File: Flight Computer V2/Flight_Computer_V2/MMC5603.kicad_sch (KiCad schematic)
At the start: 8 parts, among them IC6 MMC5603NJ

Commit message: finalized schematic, added datasheets, and pdf of schematic
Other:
- company: (none) -> By: Dylan Haussecker
- title: (none) -> Avionics Flight Computer
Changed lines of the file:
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@@
 (kicad_sch (version 20230121) (generator eeschema)
   (paper "A4")
+  (title_block
+    (title "Avionics Flight Computer")
+    (date "2023-09-04")
+    (rev "1.0")
+    (company "By: Dylan Haussecker")
+  )
   (junction (at 173.99 90.17) (diameter 0) (color 0 0 0 0)
   )

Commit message: updated pcb
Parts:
- C20: footprint (none) -> Capacitor_SMD:C_0603_1608Metric
- IC6: footprint MMC5603NJ -> LibraryLoader:MMC5603NJ
- JP3: footprint (none) -> Jumper:SolderJumper-2_P1.3mm_Open_Pad1.0x1.5mm
- R22: footprint (none) -> Resistor_SMD:R_0402_1005Metric
- R23: footprint (none) -> Resistor_SMD:R_01005_0402Metric
- TP3: footprint (none) -> TestPoint:TestPoint_Pad_D1.0mm
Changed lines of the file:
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@@
       (effects (font (size 1.27 1.27)))
     )
-    (property "Footprint" "MMC5603NJ" (at 149.86 87.63 0)
+    (property "Footprint" "LibraryLoader:MMC5603NJ" (at 149.86 87.63 0)
       (effects (font (size 1.27 1.27)) (justify left) hide)
     )
@@
       (effects (font (size 1.27 1.27)) (justify left))
     )
-    (property "Footprint" "" (at 190.5 83.82 0)
+    (property "Footprint" "Resistor_SMD:R_01005_0402Metric" (at 190.5 83.82 0)
       (effects (font (size 1.27 1.27)) hide)
     )
@@
       (effects (font (size 1.27 1.27)))
     )
-    (property "Footprint" "" (at 180.34 90.17 0)
+    (property "Footprint" "Jumper:SolderJumper-2_P1.3mm_Open_Pad1.0x1.5mm" (at 180.34 90.17 0)
       (effects (font (size 1.27 1.27)) hide)
     )
@@
       (effects (font (size 1.27 1.27)) (justify left) hide)
     )
-    (property "Footprint" "" (at 179.07 88.9 0)
+    (property "Footprint" "TestPoint:TestPoint_Pad_D1.0mm" (at 179.07 88.9 0)
       (effects (font (size 1.27 1.27)) hide)
     )
@@
       (effects (font (size 1.27 1.27)) (justify left))
     )
-    (property "Footprint" "" (at 158.75 83.82 0)
+    (property "Footprint" "Resistor_SMD:R_0402_1005Metric" (at 158.75 83.82 0)
       (effects (font (size 1.27 1.27)) hide)
     )
@@
       (effects (font (size 1.27 1.27)) (justify left) hide)
     )
-    (property "Footprint" "" (at 200.66 91.44 0)
+    (property "Footprint" "TestPoint:TestPoint_Pad_D1.0mm" (at 200.66 91.44 0)
       (effects (font (size 1.27 1.27)) hide)
     )
@@
       (effects (font (size 1.27 1.27)) (justify left))
     )
-    (property "Footprint" "" (at 128.27 102.87 0)
+    (property "Footprint" "Capacitor_SMD:C_0603_1608Metric" (at 128.27 102.87 0)
       (effects (font (size 1.27 1.27)) hide)
     )
@@
       (effects (font (size 1.27 1.27)))
     )
-    (property "Footprint" "" (at 201.93 92.71 0)
-      (effects (font (size 1.27 1.27)) hide)
-    )
+    (property "Footprint" "Jumper:SolderJumper-2_P1.3mm_Open_Pad1.0x1.5mm" (at 201.93 92.71 0)
+      (effects (font (size 1.27 1.27)) hide)
+    )

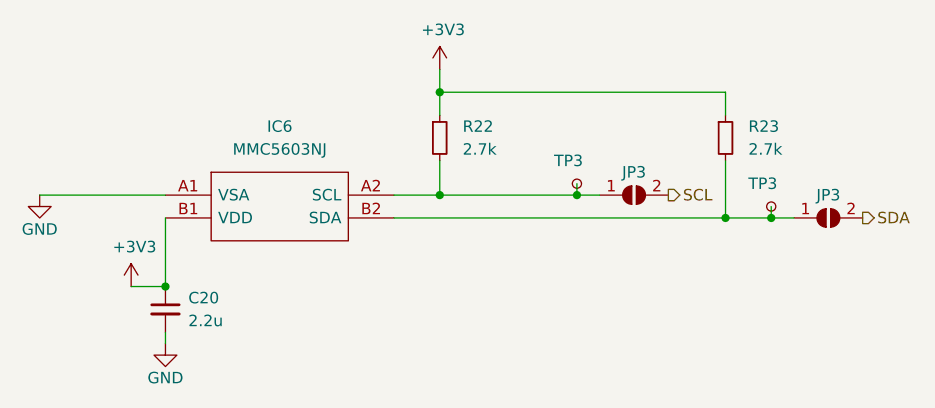
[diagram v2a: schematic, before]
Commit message: changed new flight computer scl resistors
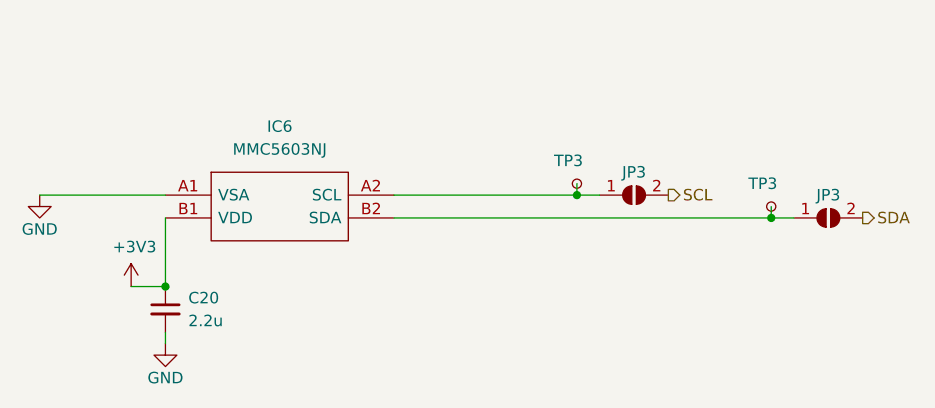
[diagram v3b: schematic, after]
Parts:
- removed R22: 2.7k, Resistor_SMD:R_0402_1005Metric, symbol Device:R_Small
- removed R23: 2.7k, Resistor_SMD:R_01005_0402Metric, symbol Device:R_Small
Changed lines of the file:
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@@
   (junction (at 173.99 90.17) (diameter 0) (color 0 0 0 0)
   )
-  (junction (at 190.5 92.71) (diameter 0) (color 0 0 0 0)
-  )
-  (junction (at 158.75 78.74) (diameter 0) (color 0 0 0 0)
-  )
   (junction (at 128.27 100.33) (diameter 0) (color 0 0 0 0)
   )
-  (junction (at 158.75 90.17) (diameter 0) (color 0 0 0 0)
-  )
   (junction (at 195.58 92.71) (diameter 0) (color 0 0 0 0)
   )
@@
     (stroke (width 0) (type default))
   )
-  (wire (pts (xy 190.5 81.28) (xy 190.5 78.74))
-    (stroke (width 0) (type default))
-  )
-  (wire (pts (xy 158.75 86.36) (xy 158.75 90.17))
-    (stroke (width 0) (type default))
-  )
   (wire (pts (xy 124.46 100.33) (xy 128.27 100.33))
     (stroke (width 0) (type default))
   )
-  (wire (pts (xy 158.75 76.2) (xy 158.75 78.74))
-    (stroke (width 0) (type default))
-  )
   (wire (pts (xy 128.27 105.41) (xy 128.27 106.68))
     (stroke (width 0) (type default))
   )
-  (wire (pts (xy 190.5 78.74) (xy 158.75 78.74))
-    (stroke (width 0) (type default))
-  )
   (wire (pts (xy 173.99 88.9) (xy 173.99 90.17))
     (stroke (width 0) (type default))
@@
     (stroke (width 0) (type default))
   )
-  (wire (pts (xy 158.75 90.17) (xy 173.99 90.17))
-    (stroke (width 0) (type default))
-  )
-  (wire (pts (xy 190.5 92.71) (xy 190.5 86.36))
+  (wire (pts (xy 153.67 90.17) (xy 173.99 90.17))
     (stroke (width 0) (type default))
   )
@@
     (stroke (width 0) (type default))
   )
-  (wire (pts (xy 190.5 92.71) (xy 195.58 92.71))
-    (stroke (width 0) (type default))
-  )
-  (wire (pts (xy 158.75 78.74) (xy 158.75 81.28))
-    (stroke (width 0) (type default))
-  )
-  (wire (pts (xy 153.67 92.71) (xy 190.5 92.71))
-    (stroke (width 0) (type default))
-  )
-  (wire (pts (xy 153.67 90.17) (xy 158.75 90.17))
+  (wire (pts (xy 153.67 92.71) (xy 195.58 92.71))
     (stroke (width 0) (type default))
   )
@@
     )
   )
-  (symbol (lib_id "Device:R_Small") (at 190.5 83.82 0) (unit 1)
-    (in_bom yes) (on_board yes) (dnp no) (fields_autoplaced)
-    (property "Reference" "R23" (at 193.04 82.55 0)
-      (effects (font (size 1.27 1.27)) (justify left))
-    )
-    (property "Value" "2.7k" (at 193.04 85.09 0)
-      (effects (font (size 1.27 1.27)) (justify left))
-    )
-    (property "Footprint" "Resistor_SMD:R_01005_0402Metric" (at 190.5 83.82 0)
-      (effects (font (size 1.27 1.27)) hide)
-    )
-    (property "Datasheet" "~" (at 190.5 83.82 0)
-      (effects (font (size 1.27 1.27)) hide)
-    )
-    (pin "1")
-    (pin "2")
-    (instances
-      (project "Flight_Computer_V2"
-        (path "/39d7ebb3-b69d-4ae9-8f55-c9acfe77d345/82e19a29-2001-4834-a54c-a35440bfa66f"
-          (reference "R23") (unit 1)
-        )
-      )
-    )
-  )
   (symbol (lib_id "Jumper:SolderJumper_2_Open") (at 180.34 90.17 0) (unit 1)
     (in_bom yes) (on_board yes) (dnp no)
@@
         (path "/b1d299c5-d712-4abd-abfc-85bf9dc0241e/b49ccfa2-a443-40e6-a4d4-e4cbe0c6bead"
           (reference "#PWR020") (unit 1)
-        )
-      )
-    )
-  )
-  (symbol (lib_id "Device:R_Small") (at 158.75 83.82 0) (unit 1)
-    (in_bom yes) (on_board yes) (dnp no) (fields_autoplaced)
-    (property "Reference" "R22" (at 161.29 82.55 0)
-      (effects (font (size 1.27 1.27)) (justify left))
-    )
-    (property "Value" "2.7k" (at 161.29 85.09 0)
-      (effects (font (size 1.27 1.27)) (justify left))
-    )
-    (property "Footprint" "Resistor_SMD:R_0402_1005Metric" (at 158.75 83.82 0)
-      (effects (font (size 1.27 1.27)) hide)
-    )
-    (property "Datasheet" "~" (at 158.75 83.82 0)
-      (effects (font (size 1.27 1.27)) hide)
-    )
-    (pin "1")
-    (pin "2")
-    (instances
-      (project "Flight_Computer_V2"
-        (path "/39d7ebb3-b69d-4ae9-8f55-c9acfe77d345/82e19a29-2001-4834-a54c-a35440bfa66f"
-          (reference "R22") (unit 1)
         )
       )
@@
         )
       )
-    )
-  )
-  (symbol (lib_id "power:+3V3") (at 158.75 76.2 0) (unit 1)
-    (in_bom yes) (on_board yes) (dnp no)
-    (property "Reference" "#PWR09" (at 158.75 80.01 0)
-      (effects (font (size 1.27 1.27)) hide)
-    )
-    (property "Value" "+3V3" (at 159.131 71.8058 0)
-      (effects (font (size 1.27 1.27)))
-    )
-    (property "Footprint" "" (at 158.75 76.2 0)
-      (effects (font (size 1.27 1.27)) hide)
-    )
-    (property "Datasheet" "" (at 158.75 76.2 0)
-      (effects (font (size 1.27 1.27)) hide)
-    )
-    (pin "1")
-    (instances
-      (project "STM32F405RGT6-Breakout"
-        (path "/0540e924-c3ed-4064-b360-826f481ae85c"
-          (reference "#PWR09") (unit 1)
-        )
-      )
-      (project "Flight_Computer_V2"
-        (path "/39d7ebb3-b69d-4ae9-8f55-c9acfe77d345/4a05f57f-ad7d-4317-b08f-5601038a99f3"
-          (reference "#PWR09") (unit 1)
-        )
-        (path "/39d7ebb3-b69d-4ae9-8f55-c9acfe77d345"
-          (reference "#PWR040") (unit 1)
-        )
-        (path "/39d7ebb3-b69d-4ae9-8f55-c9acfe77d345/82e19a29-2001-4834-a54c-a35440bfa66f"
-          (reference "#PWR059") (unit 1)
-        )
-      )
-      (project "STM32F405RGT6"
-        (path "/6135eb53-87c0-4516-a6dc-aa2a3e58fdeb"
-          (reference "#PWR02") (unit 1)
-        )
-      )
